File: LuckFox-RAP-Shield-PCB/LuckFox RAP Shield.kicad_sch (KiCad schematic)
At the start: 4 parts, among them J1 LuckFox_Pico_Mini_Connector, J2 External_5V_Input_from_Buck_M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, U2 W5500_Ethernet_Module_DNP_on_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

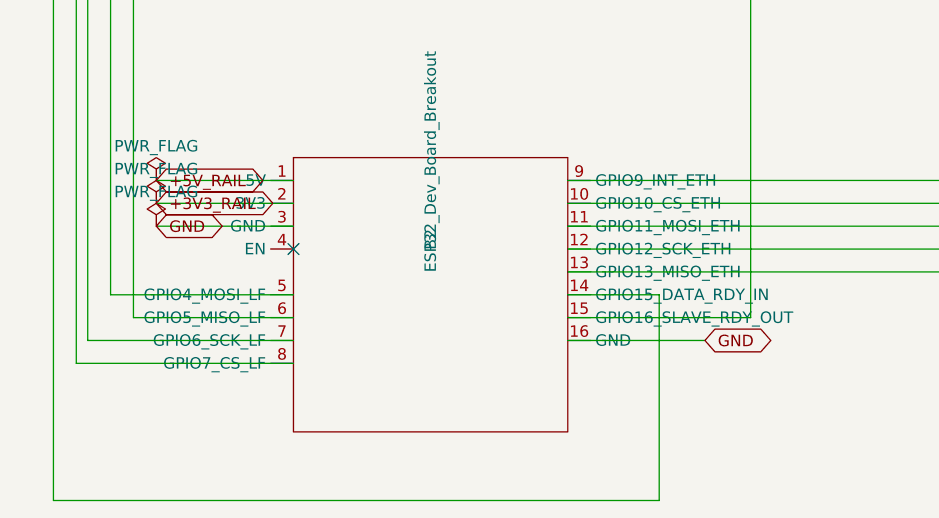
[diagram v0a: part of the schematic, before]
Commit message: Reroute LuckFox SPI net swap onto real copper, fix GND edge routing, flip headers bottom-only
Routes the 8 swapped LF/ETH SPI nets (J1/B2/U2 pads renamed in a prior
commit but left as ratsnest) as real 0.2mm traces. Reworks the GND
connection from J1's two GND pads to the board's zone fill -- earlier
routing detoured all the way to the board's far corners and briefly ran
copper over the open LuckFox nesting-slot cutout with no substrate
underneath; now a short, direct stub into the nearby fill next to B2's own
GND pad. Also flips ESP32 (B2), the Ethernet header (U2), and the power
header (J2) to bottom-only solder-mask exposure, matching how they're
actually soldered.

Co-Authored-By: Claude Sonnet 5 <noreply@anthropic.com>
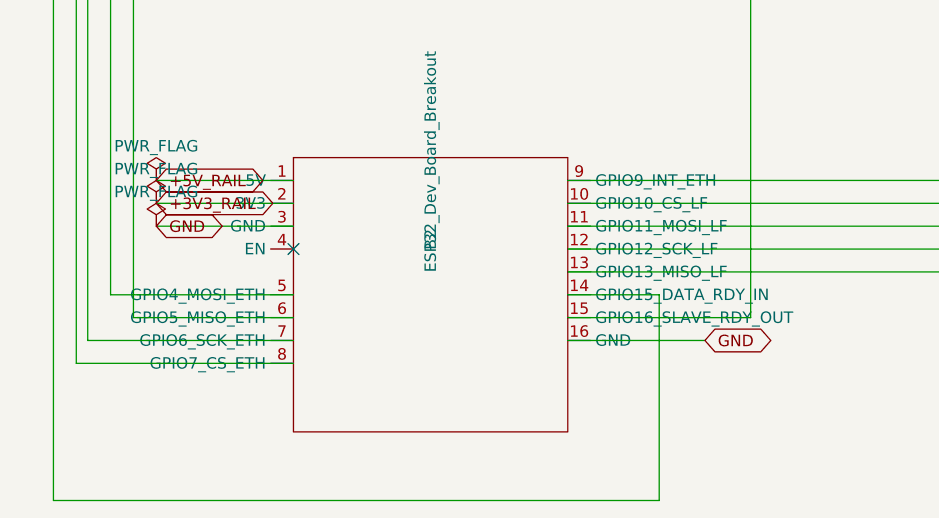
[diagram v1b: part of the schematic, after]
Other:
- moved on the sheet: B2

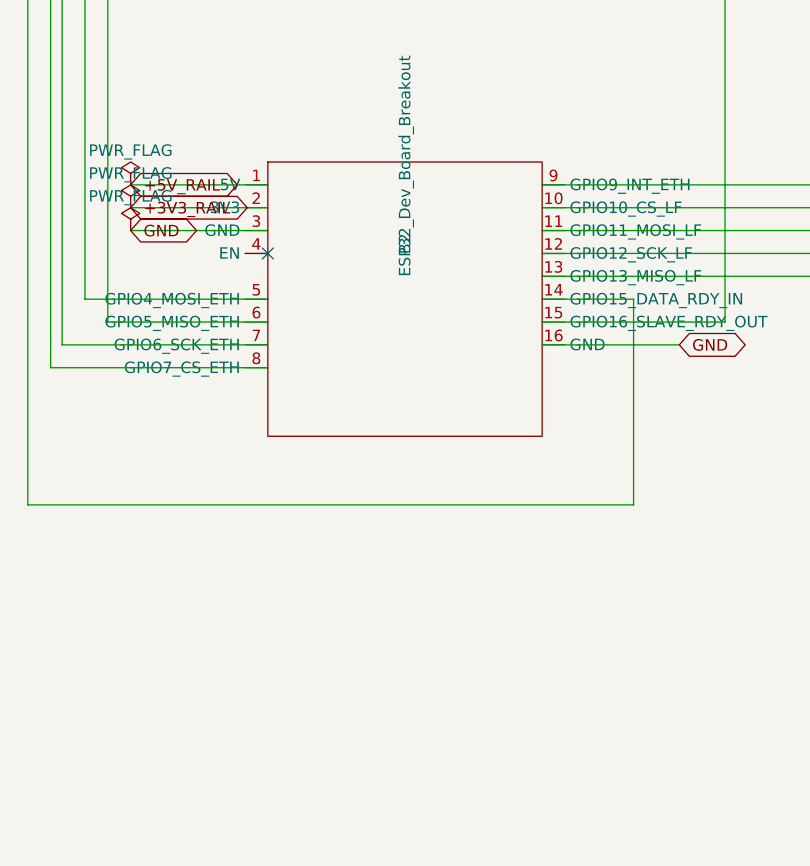
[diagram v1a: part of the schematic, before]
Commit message: Push PCB copper/mask/edge clearance to manufacturer spec where physically possible
Compared the board against a manufacturer's stated minimums (track/space,
via size, solder mask expansion, edge clearance, silkscreen line width)
and pushed each toward spec via DRC bisection rather than guessing:

- Solder mask expansion: 0 -> 0.095mm (spec 0.1016mm; verified safe max)
- Board edge clearance: 0 -> 0.254mm, extending the existing J1
  castellated-pad DRU exception to the GND/+5V_RAIL/GPIO15/16 nets that
  approach the same by-design edge zone (previously unflagged only
  because the global minimum was 0, not because they were actually clear)
- Track width / clearance / via size: confirmed via bisection to already
  sit at this layout's true physical ceiling (0.2mm / 0.2mm / 0.8mm) --
  the B2 header has zero spare copper margin, and pushing further
  reintroduces real short-circuit risk (shorting_items/solder_mask_bridge
  DRC errors), so left at their original values rather than forced
- Silkscreen minimum line width: attempted, reverted -- meeting it
  required growing pin-label text past the point where it stays clear of
  the module outline and board edge on this densely-labeled breakout
  footprint, trading a spec item that wasn't actually required (only
  line width was, not silk-to-silk/edge spacing) for new DRC warnings
  that didn't exist before

0 DRC errors. Also confirmed clearance/shorting/track-width checks are
already default "error" severity, not something needing manual opt-in.

Co-Authored-By: Claude Sonnet 5 <noreply@anthropic.com>
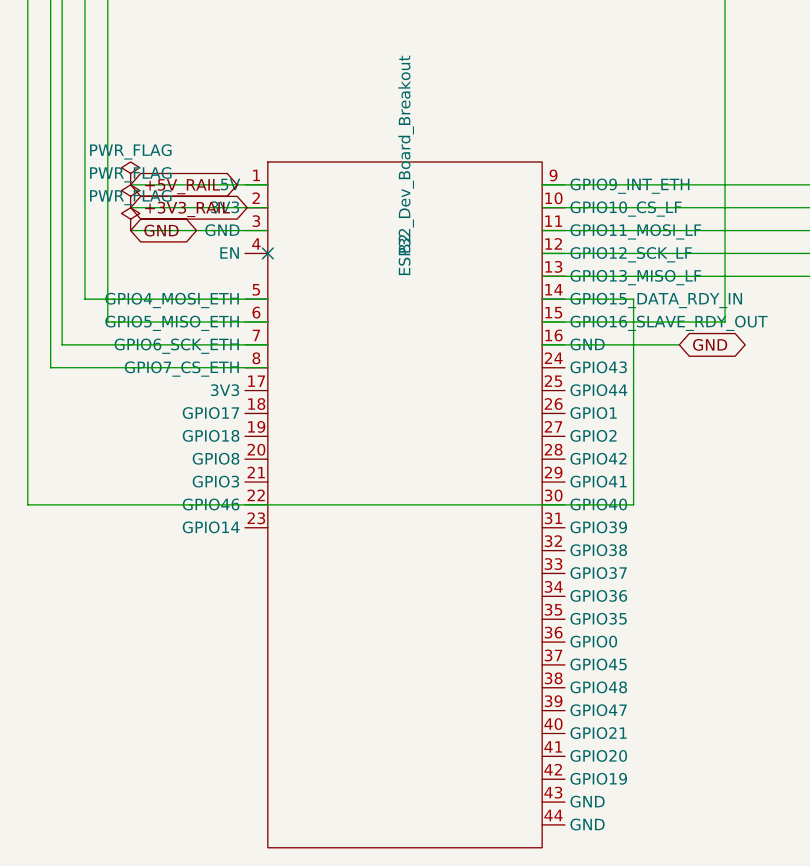
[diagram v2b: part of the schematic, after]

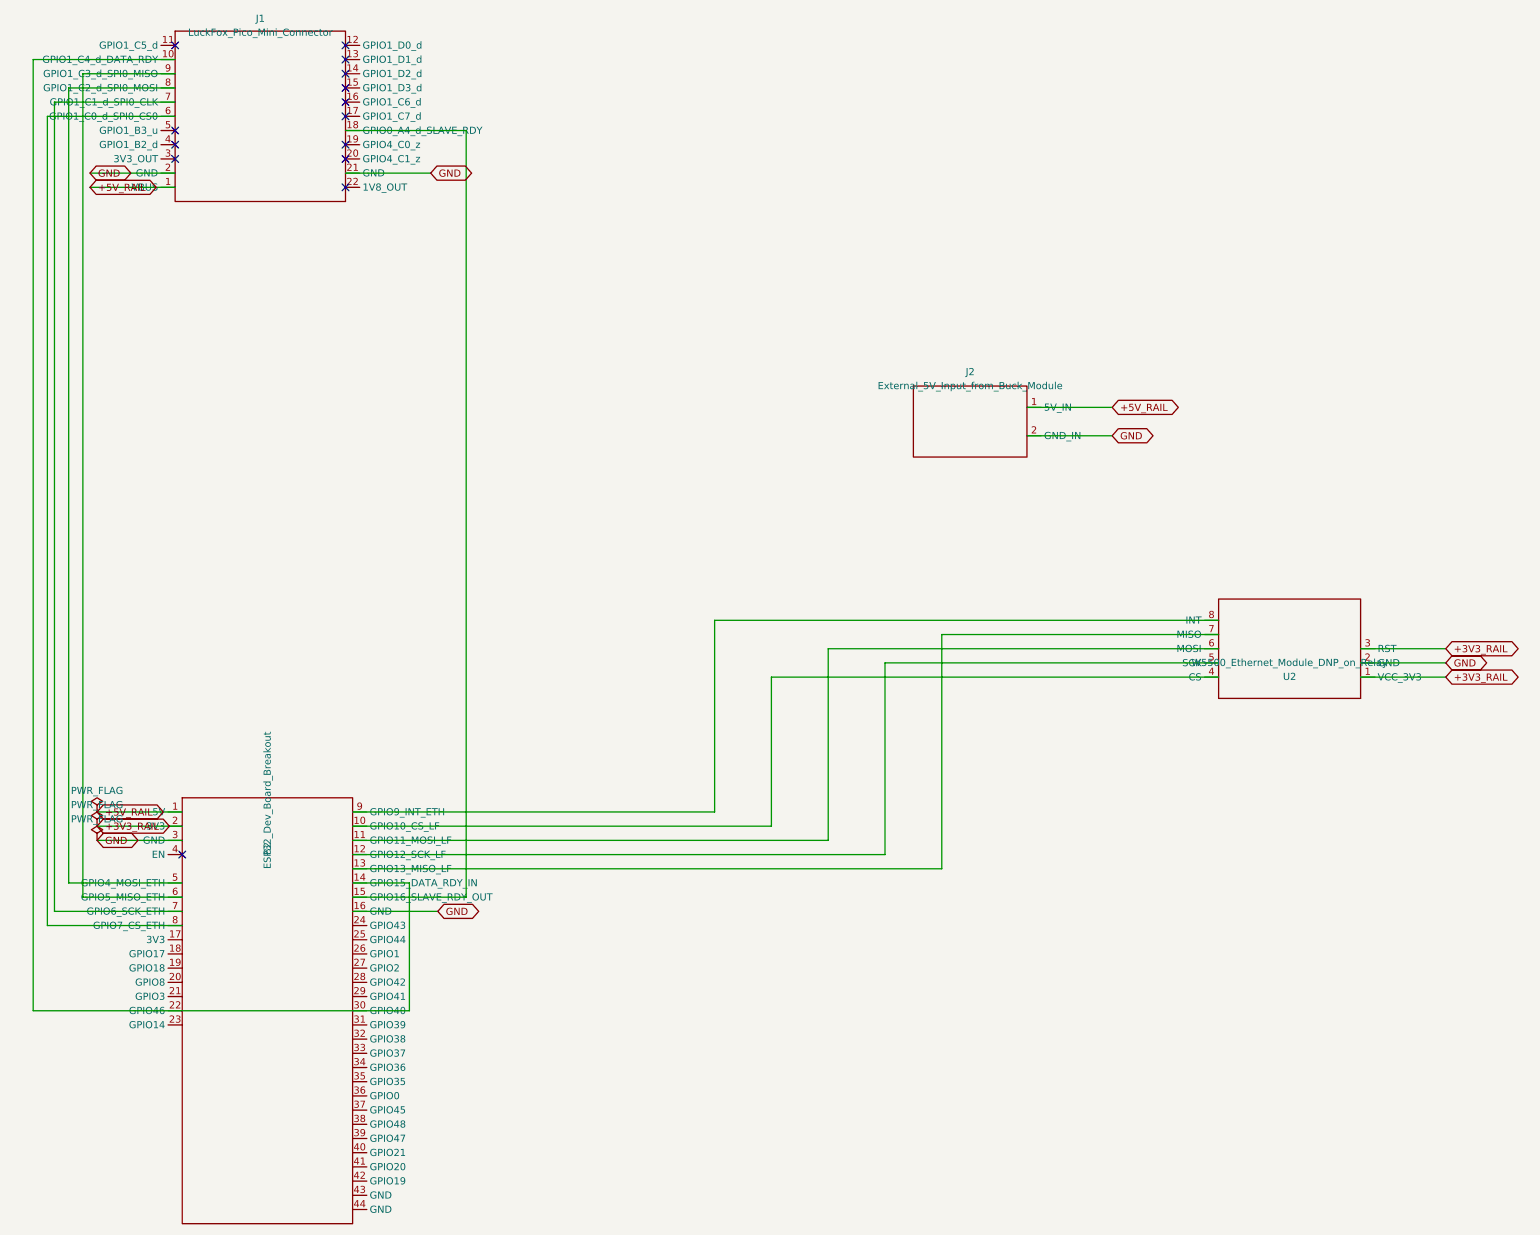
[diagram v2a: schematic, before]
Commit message: Fix W5500 SPI net mixup, bring copper fully to manufacturer spec, polish silkscreen
- Schematic: W5500's CS/SCK/MOSI/MISO were wired to the same ESP32 GPIO
  group LuckFox uses (Net-(B2-GPIO10-13_..._LF)) instead of its own
  dedicated group (GPIO4/5/6/7/9_..._ETH) -- real short/bus-conflict risk,
  not a false positive. Rewired to the correct pins.
- Reference designators B2/J1 had been accidentally renamed (to
  "ESP32-S3-Devkitc-1"/"Luckfox Pico Mini"), silently breaking the DRU
  exception that protects J1's spare castellated pads from false edge-
  clearance errors. Restored to "B2"/"J1".
- Copper brought to full manufacturer spec via real re-routing (not just
  loosened settings) -- track width 0.2->0.254mm, clearance 0.2->0.254mm,
  via 0.8/0.4->1.37-1.47mm/1mm (vias now sized/centered so their own
  drilled hole forms a proper semicircular castellation edge alongside
  LuckFox's own, once routed), solder mask expansion 0->0.1016mm, board
  edge clearance 0->0.254mm (extended the existing J1 DRU exception to
  the GND/+5V_RAIL/GPIO15/16 nets that share the same edge zone), zone
  min_thickness 0.25->0.254mm. All verified via DRC bisection against
  real geometry, including a proper --refill-zones pass each time (a
  plain width edit doesn't recompute the pour shape, which produced
  false zone-clearance violations during testing).
- Silkscreen line width and text thickness both brought to the 0.203mm
  spec. Text needed a wider stroke *and* larger character size together,
  since KiCad clamps effective stroke thickness to 25% of character
  height -- thickness alone was silently capped by the original 0.8mm
  size.
- Enlarged the board logo 1.2x (silhouette only, kept the original
  0.203mm line weight instead of scaling it 1:1, which read as too
  heavy), and made the 4 mounting holes symmetric on both axes with
  clean rounded coordinates (117/154 x, 78.9/134.3 y).

0 DRC errors, every numeric item on the target manufacturer's spec sheet
now met with real m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
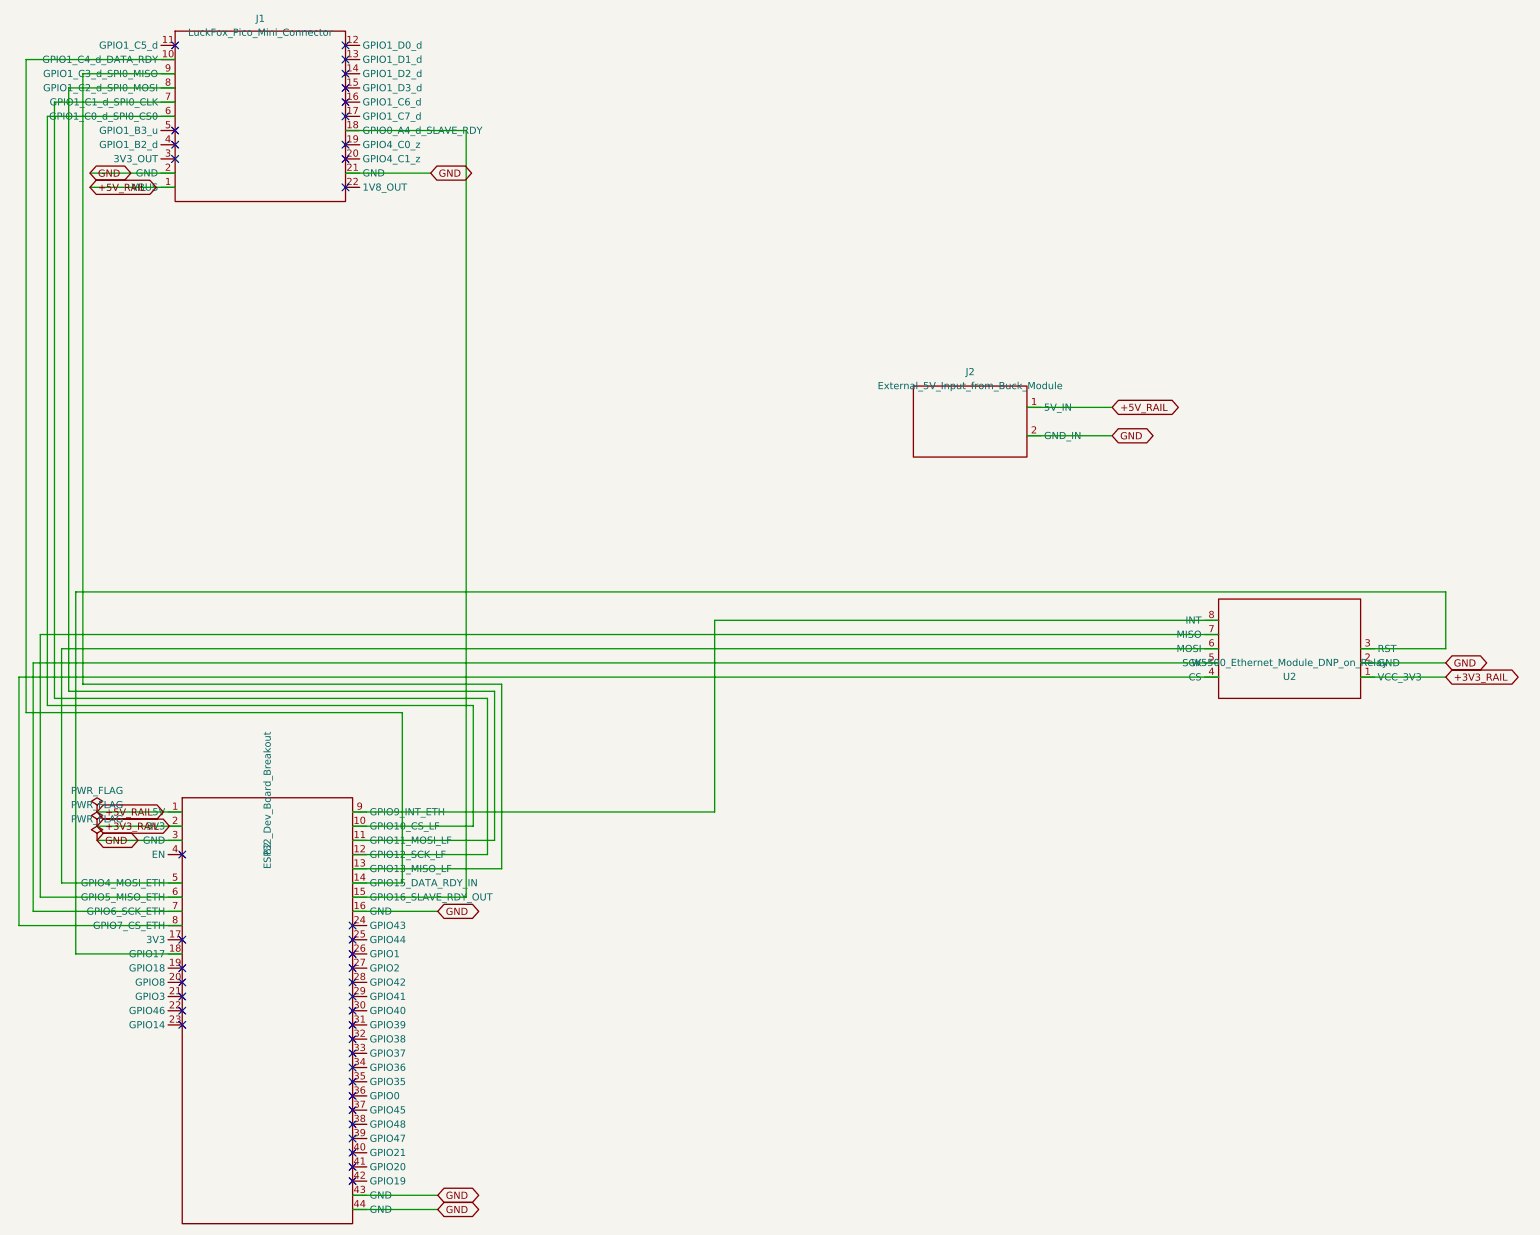
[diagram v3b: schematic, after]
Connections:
- net +3V3_RAIL: no longer U2.3 (RST)
- net GND: now also B2.43 (GND), B2.44 (GND)
- net at B2.10 (GPIO10_CS_LF): now also J1.6 (GPIO1_C0_d_SPI0_CS0); no longer U2.4 (CS)
- net at B2.11 (GPIO11_MOSI_LF): now also J1.8 (GPIO1_C2_d_SPI0_MOSI); no longer U2.6 (MOSI)
- net at B2.12 (GPIO12_SCK_LF): now also J1.7 (GPIO1_C1_d_SPI0_CLK); no longer U2.5 (SCK)
- net at B2.13 (GPIO13_MISO_LF): now also J1.9 (GPIO1_C3_d_SPI0_MISO); no longer U2.7 (MISO)
- net at B2.18 (GPIO17): now also U2.3 (RST)
- net at B2.5 (GPIO4_MOSI_ETH): now also U2.6 (MOSI); no longer J1.8 (GPIO1_C2_d_SPI0_MOSI)
- net at B2.6 (GPIO5_MISO_ETH): now also U2.7 (MISO); no longer J1.9 (GPIO1_C3_d_SPI0_MISO)
- net at B2.7 (GPIO6_SCK_ETH): now also U2.5 (SCK); no longer J1.7 (GPIO1_C1_d_SPI0_CLK)
- net at B2.8 (GPIO7_CS_ETH): now also U2.4 (CS); no longer J1.6 (GPIO1_C0_d_SPI0_CS0)
- no-connect marks 14 -> 39
